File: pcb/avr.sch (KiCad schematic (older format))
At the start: 36 parts, among them IC201 MCU-ATMEGA328P-MU_QFN32_, J201 CONN_02X03, J202 jumper, P201 CONNECTOR, P202 CONNECTOR, P203 CONNECTOR, P204 CONNECTOR, P205 CONNECTOR, P206 CONNECTOR, P207 CONNECTOR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

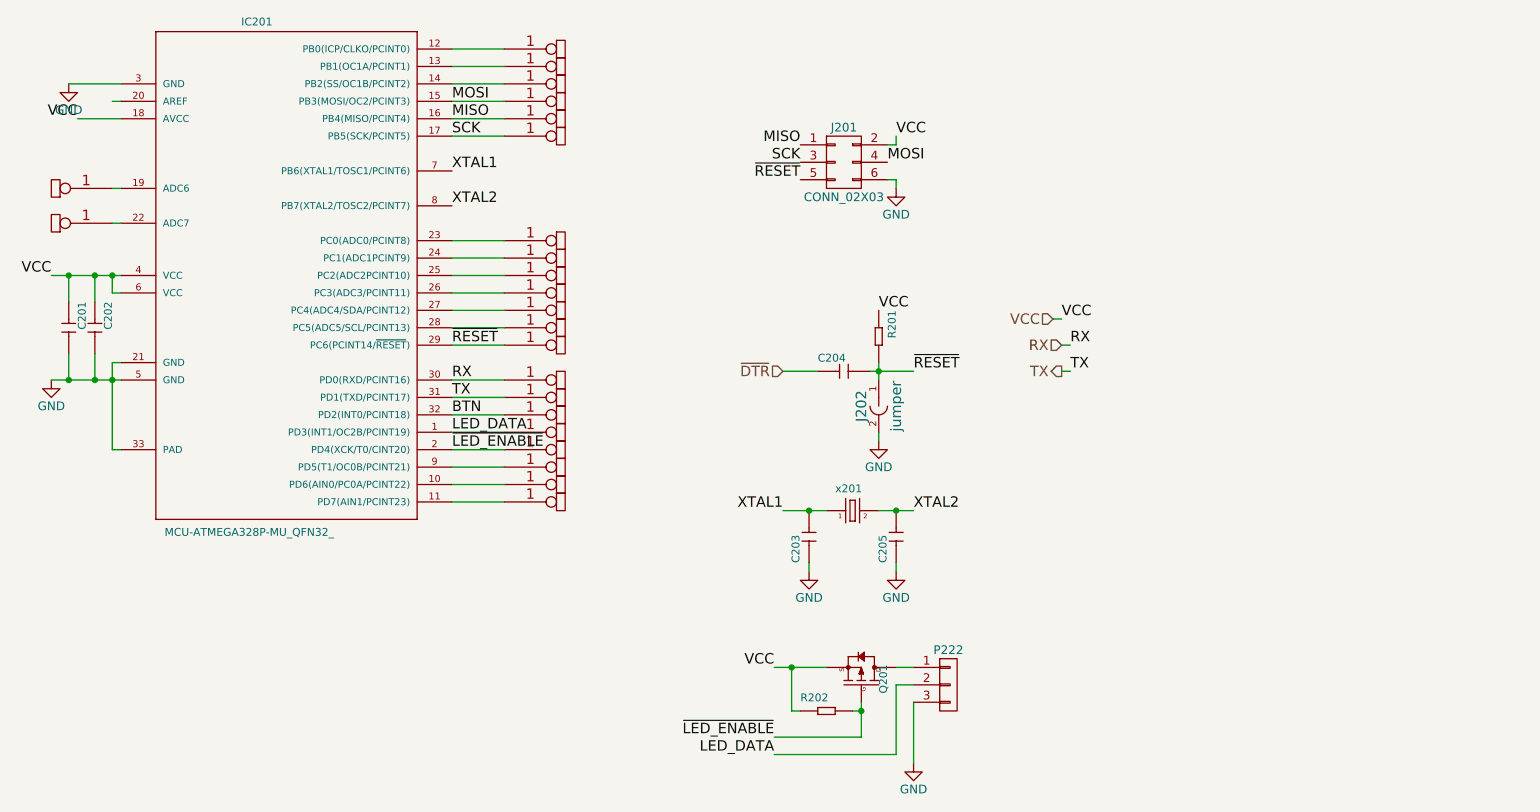
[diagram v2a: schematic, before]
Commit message: added button, capacitor to led strip power and jumpers to external rx/tx. everything layed out and connected
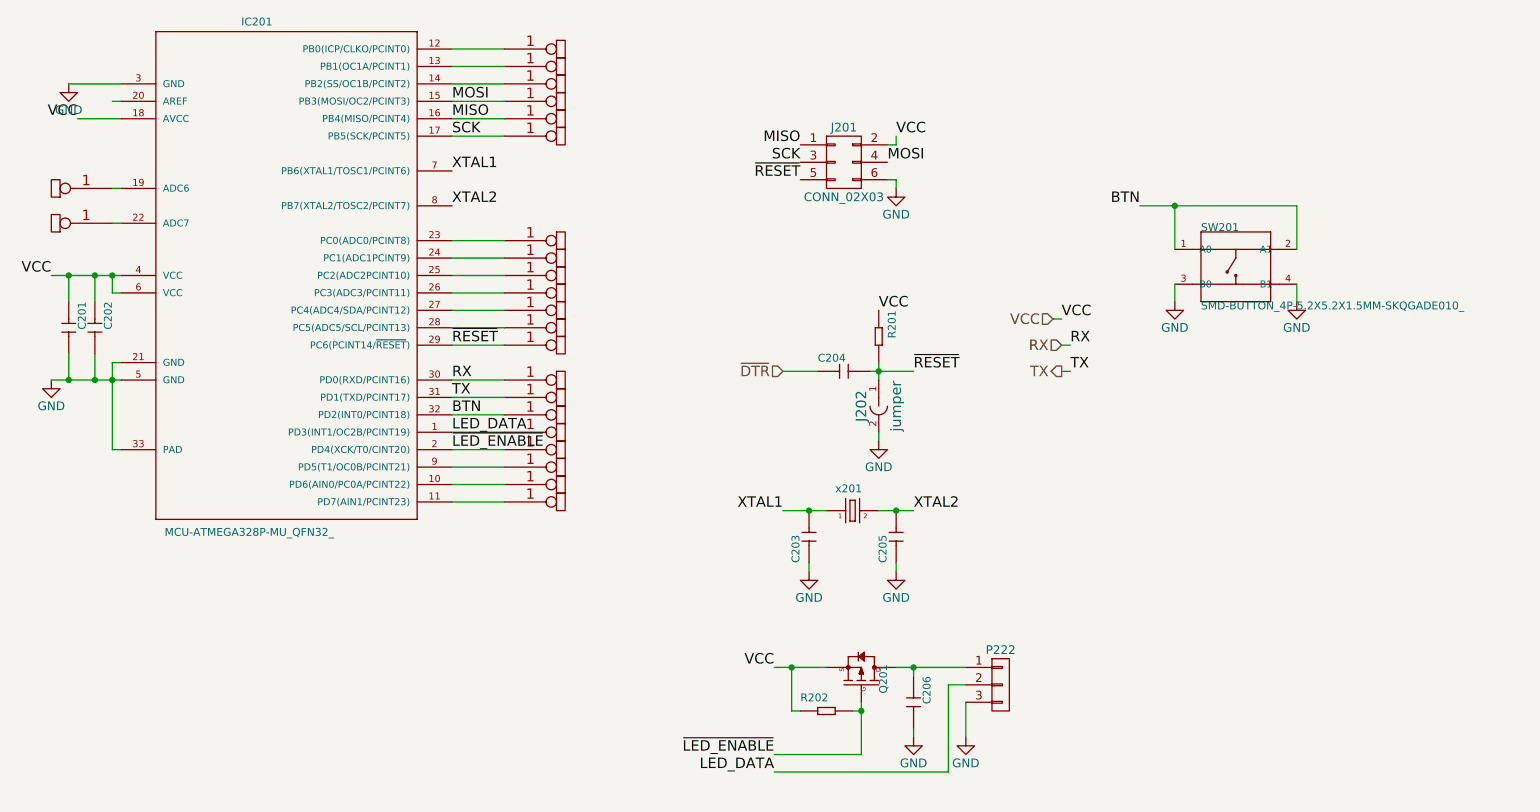
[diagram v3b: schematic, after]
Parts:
- added C206: CERAMIC-22UF-6.3V-20%-X5R_0805_, netl:C0805, symbol CERAMIC-22UF-6.3V-20%-X5R_0805_
- added SW201: SMD-BUTTON_4P-5.2X5.2X1.5MM-SKQGADE010_, SeeedOPL-Switch-2016:SW4-SMD-5.2X5.2X1.5MM, symbol SMD-BUTTON_4P-5.2X5.2X1.5MM-SKQGADE010_
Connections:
- net BTN: now also SW201.1 (A0), SW201.2 (A1)
- net GND: now also C206.2, SW201.3 (B0), SW201.4 (B1)
- net at P222.1 (P1), Q201.3 (D): now also C206.1
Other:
- moved on the sheet: P222
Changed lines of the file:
@@
 L CONN_01X03 P222
 U 1 1 58BAB28B
-P 8250 5800
-F 0 "P222" H 8250 6000 50  0000 C CNN
-F 1 "CONN_01X03" V 8350 5800 50  0001 C CNN
-F 2 "netl:SM_3_WIRE" H 8250 5800 50  0001 C CNN
-F 3 "" H 8250 5800 50  0000 C CNN
-	1    8250 5800
-	1    0    0    -1
-$EndComp
-$Comp
-L GND #PWR207
+P 8550 5800
+F 0 "P222" H 8550 6000 50  0000 C CNN
+F 1 "CONN_01X03" V 8650 5800 50  0001 C CNN
+F 2 "netl:SM_3_WIRE" H 8550 5800 50  0001 C CNN
+F 3 "" H 8550 5800 50  0000 C CNN
+	1    8550 5800
+	1    0    0    -1
+$EndComp
+$Comp
+L GND #PWR05
 U 1 1 58BAB3DE
-P 8050 6250
-F 0 "#PWR207" H 8050 6000 50  0001 C CNN
-F 1 "GND" H 8050 6100 50  0000 C CNN
-F 2 "" H 8050 6250 50  0000 C CNN
-F 3 "" H 8050 6250 50  0000 C CNN
-	1    8050 6250
-	1    0    0    -1
-$EndComp
-Text Label 7250 6200 2    60   ~ 0
+P 8350 6100
+F 0 "#PWR05" H 8350 5850 50  0001 C CNN
+F 1 "GND" H 8350 5950 50  0000 C CNN
+F 2 "" H 8350 6100 50  0000 C CNN
+F 3 "" H 8350 6100 50  0000 C CNN
+	1    8350 6100
+	1    0    0    -1
+$EndComp
+Text Label 7250 6300 2    60   ~ 0
 LED_DATA
 $Comp
@@
 $EndComp
 $Comp
-L GND #PWR206
+L GND #PWR06
 U 1 1 5A3AC4B3
 P 7950 5150
-F 0 "#PWR206" H 7950 4900 50  0001 C CNN
+F 0 "#PWR06" H 7950 4900 50  0001 C CNN
 F 1 "GND" H 7950 5000 50  0000 C CNN
 F 2 "" H 7950 5150 50  0000 C CNN
@@
 $EndComp
 $Comp
-L GND #PWR203
+L GND #PWR07
 U 1 1 5A3AC530
 P 7450 5150
-F 0 "#PWR203" H 7450 4900 50  0001 C CNN
+F 0 "#PWR07" H 7450 4900 50  0001 C CNN
 F 1 "GND" H 7450 5000 50  0000 C CNN
 F 2 "" H 7450 5150 50  0000 C CNN
@@
 $EndComp
 $Comp
-L GND #PWR201
+L GND #PWR08
 U 1 1 5A3AD1F6
 P 3100 4050
-F 0 "#PWR201" H 3100 3800 50  0001 C CNN
+F 0 "#PWR08" H 3100 3800 50  0001 C CNN
 F 1 "GND" H 3100 3900 50  0000 C CNN
 F 2 "" H 3100 4050 50  0001 C CNN
@@
 $EndComp
 $Comp
-L GND #PWR202
+L GND #PWR09
 U 1 1 5A3AE5DA
 P 3200 2350
-F 0 "#PWR202" H 3200 2100 50  0001 C CNN
+F 0 "#PWR09" H 3200 2100 50  0001 C CNN
 F 1 "GND" H 3200 2200 50  0000 C CNN
 F 2 "" H 3200 2350 50  0001 C CNN
@@
 SCK
 $Comp
-L GND #PWR205
+L GND #PWR010
 U 1 1 5A551E4E
 P 7950 2950
-F 0 "#PWR205" H 7950 2700 50  0001 C CNN
+F 0 "#PWR010" H 7950 2700 50  0001 C CNN
 F 1 "GND" H 7950 2800 50  0000 C CNN
 F 2 "" H 7950 2950 50  0000 C CNN
@@
 	1    0    0    -1
 $EndComp
-Wire Wire Line
-	8050 5900 8050 6250
-Wire Wire Line
-	7950 5800 8050 5800
-Wire Wire Line
-	7950 5700 8050 5700
-Wire Wire Line
-	7300 4800 7550 4800
-Wire Wire Line
-	7850 4800 8050 4800
-Wire Wire Line
-	7450 5100 7450 5150
-Wire Wire Line
-	7950 5100 7950 5150
-Connection ~ 7450 4800
-Connection ~ 7950 4800
-Wire Wire Line
-	3100 3450 3500 3450
-Wire Wire Line
-	3200 3600 3200 3450
-Connection ~ 3200 3450
-Wire Wire Line
-	3350 3600 3350 3450
-Connection ~ 3350 3450
-Wire Wire Line
-	3500 3550 3450 3550
-Wire Wire Line
-	3450 3550 3450 3450
-Connection ~ 3450 3450
-Wire Wire Line
-	3100 4050 3500 4050
-Wire Wire Line
-	3200 3900 3200 4050
-Connection ~ 3200 4050
-Wire Wire Line
-	3350 3900 3350 4050
-Connection ~ 3350 4050
-Wire Wire Line
-	3500 3950 3450 3950
-Wire Wire Line
-	3450 3950 3450 4450
-Connection ~ 3450 4050
-Wire Wire Line
-	3500 2350 3200 2350
-Wire Wire Line
-	5400 4050 5700 4050
-Wire Wire Line
-	5400 4150 5700 4150
-Wire Wire Line
-	7850 3950 7850 4050
-Wire Wire Line
-	7800 4000 8050 4000
-Connection ~ 7850 4000
-Wire Wire Line
-	7500 4000 7300 4000
-Wire Wire Line
-	5700 4250 5400 4250
-Wire Wire Line
-	5400 4350 5700 4350
-Wire Wire Line
-	5700 4450 5400 4450
-Wire Wire Line
-	5400 4550 5700 4550
-Wire Wire Line
-	5700 4650 5400 4650
-Wire Wire Line
-	5400 4750 5700 4750
-Wire Wire Line
-	5400 3850 5700 3850
-Wire Wire Line
-	5400 3750 5700 3750
-Wire Wire Line
-	5700 3650 5400 3650
-Wire Wire Line
-	5400 3550 5700 3550
-Wire Wire Line
-	5700 3450 5400 3450
-Wire Wire Line
-	5400 3350 5700 3350
-Wire Wire Line
-	5700 3250 5400 3250
-Wire Wire Line
-	5400 2650 5700 2650
-Wire Wire Line
-	5700 2550 5400 2550
-Wire Wire Line
-	5400 2450 5700 2450
-Wire Wire Line
-	5700 2350 5400 2350
-Wire Wire Line
-	5400 2250 5700 2250
-Wire Wire Line
-	5700 2150 5400 2150
-Wire Wire Line
-	3500 2950 3450 2950
-Wire Wire Line
-	3450 3150 3500 3150
-Wire Wire Line
-	8900 3850 8950 3850
-Wire Wire Line
-	8900 4000 8950 4000
-Wire Wire Line
-	3450 4450 3500 4450
-Wire Wire Line
-	7950 2950 7950 2900
-Wire Wire Line
-	7950 2900 7900 2900
-Wire Wire Line
-	7950 2650 7950 2700
-Wire Wire Line
-	7950 2700 7900 2700
-Wire Wire Line
-	8850 3700 8900 3700
-Wire Wire Line
-	7250 5700 7550 5700
-Wire Wire Line
-	7750 5900 7750 6100
-Wire Wire Line
-	7750 5950 7700 5950
-Wire Wire Line
-	7400 5950 7350 5950
-Wire Wire Line
-	7350 5950 7350 5700
-Connection ~ 7350 5700
-Wire Wire Line
-	7750 6100 7250 6100
-Connection ~ 7750 5950
-Text Label 7250 6100 2    60   ~ 0
+Text Label 7250 6200 2    60   ~ 0
 ~LED_ENABLE
 Text Label 5400 4450 0    60   ~ 0
@@
 $EndComp
 $Comp
-L GND #PWR204
+L GND #PWR011
 U 1 1 5A566D1F
 P 7850 4400
-F 0 "#PWR204" H 7850 4150 50  0001 C CNN
+F 0 "#PWR011" H 7850 4150 50  0001 C CNN
 F 1 "GND" H 7850 4250 50  0000 C CNN
 F 2 "" H 7850 4400 50  0000 C CNN
@@
 	1    0    0    -1
 $EndComp
+$Comp
+L SMD-BUTTON_4P-5.2X5.2X1.5MM-SKQGADE010_ SW201
+U 1 1 5A78AF11
+P 9900 3400
+F 0 "SW201" H 9700 3600 45  0000 L BNN
+F 1 "SMD-BUTTON_4P-5.2X5.2X1.5MM-SKQGADE010_" H 9700 3150 45  0000 L BNN
+F 2 "SeeedOPL-Switch-2016:SW4-SMD-5.2X5.2X1.5MM" H 9900 3400 60  0001 C CNN
+F 3 "" H 9900 3400 60  0001 C CNN
+F 4 "SKQGADE010" H 9930 3550 20  0001 C CNN "MPN"
+F 5 "311020017" H 9930 3550 20  0001 C CNN "SKU"
+	1    9900 3400
+	1    0    0    -1
+$EndComp
+Wire Wire Line
+	8350 5900 8350 6100
+Wire Wire Line
+	8250 5800 8350 5800
+Wire Wire Line
+	7950 5700 8350 5700
+Wire Wire Line
+	7300 4800 7550 4800
+Wire Wire Line
+	7850 4800 8050 4800
+Wire Wire Line
+	7450 5100 7450 5150
+Wire Wire Line
+	7950 5100 7950 5150
+Connection ~ 7450 4800
+Connection ~ 7950 4800
+Wire Wire Line
+	3100 3450 3500 3450
+Wire Wire Line
+	3200 3600 3200 3450
+Connection ~ 3200 3450
+Wire Wire Line
+	3350 3600 3350 3450
+Connection ~ 3350 3450
+Wire Wire Line
+	3500 3550 3450 3550
+Wire Wire Line
+	3450 3550 3450 3450
+Connection ~ 3450 3450
+Wire Wire Line
+	3100 4050 3500 4050
+Wire Wire Line
+	3200 3900 3200 4050
+Connection ~ 3200 4050
+Wire Wire Line
+	3350 3900 3350 4050
+Connection ~ 3350 4050
+Wire Wire Line
+	3500 3950 3450 3950
+Wire Wire Line
+	3450 3950 3450 4450
+Connection ~ 3450 4050
+Wire Wire Line
+	3500 2350 3200 2350
+Wire Wire Line
+	5400 4050 5700 4050
+Wire Wire Line
+	5400 4150 5700 4150
+Wire Wire Line
+	7850 3950 7850 4050
+Wire Wire Line
+	7800 4000 8050 4000
+Connection ~ 7850 4000
+Wire Wire Line
+	7500 4000 7300 4000
+Wire Wire Line
+	5700 4250 5400 4250
+Wire Wire Line
+	5400 4350 5700 4350
+Wire Wire Line
+	5700 4450 5400 4450
+Wire Wire Line
+	5400 4550 5700 4550
+Wire Wire Line
+	5700 4650 5400 4650
+Wire Wire Line
+	5400 4750 5700 4750
+Wire Wire Line
+	5400 3850 5700 3850
+Wire Wire Line
+	5400 3750 5700 3750
+Wire Wire Line
+	5700 3650 5400 3650
+Wire Wire Line
+	5400 3550 5700 3550
+Wire Wire Line
+	5700 3450 5400 3450
+Wire Wire Line
+	5400 3350 5700 3350
+Wire Wire Line
+	5700 3250 5400 3250
+Wire Wire Line
+	5400 2650 5700 2650
+Wire Wire Line
+	5700 2550 5400 2550
+Wire Wire Line
+	5400 2450 5700 2450
+Wire Wire Line
+	5700 2350 5400 2350
+Wire Wire Line
+	5400 2250 5700 2250
+Wire Wire Line
+	5700 2150 5400 2150
+Wire Wire Line
+	3500 2950 3450 2950
+Wire Wire Line
+	3450 3150 3500 3150
+Wire Wire Line
+	8900 3850 8950 3850
+Wire Wire Line
+	8900 4000 8950 4000
+Wire Wire Line
+	3450 4450 3500 4450
+Wire Wire Line
+	7950 2950 7950 2900
+Wire Wire Line
+	7950 2900 7900 2900
+Wire Wire Line
+	7950 2650 7950 2700
+Wire Wire Line
+	7950 2700 7900 2700
+Wire Wire Line
+	8850 3700 8900 3700
+Wire Wire Line
+	7250 5700 7550 5700
+Wire Wire Line
+	7750 5900 7750 6200
+Wire Wire Line
+	7750 5950 7700 5950
+Wire Wire Line
+	7400 5950 7350 5950
+Wire Wire Line
+	7350 5950 7350 5700
+Connection ~ 7350 5700
+Wire Wire Line
+	7750 6200 7250 6200
+Connection ~ 7750 5950
 Wire Wire Line
 	7850 4350 7850 4400
 Wire Wire Line
-	7250 6200 7950 6200
-Wire Wire Line
-	7950 6200 7950 5800
+	7250 6300 8250 6300
+Wire Wire Line
+	8250 6300 8250 5800
 Wire Wire Line
 	3250 2550 3500 2550
 Wire Wire Line
 	3500 2450 3450 2450
+Wire Wire Line
+	10250 3050 10250 3300
+Wire Wire Line
+	9350 3050 10250 3050
+Wire Wire Line
+	9550 3050 9550 3300
+Connection ~ 9550 3050
+Text Label 9350 3050 2    60   ~ 0
+BTN
+$Comp
+L GND #PWR012
+U 1 1 5A78B21A
+P 9550 3600
+F 0 "#PWR012" H 9550 3350 50  0001 C CNN
+F 1 "GND" H 9550 3450 50  0000 C CNN
+F 2 "" H 9550 3600 50  0000 C CNN
+F 3 "" H 9550 3600 50  0000 C CNN
+	1    9550 3600
+	1    0    0    -1
+$EndComp
+$Comp
+L GND #PWR013
+U 1 1 5A78B24F
+P 10250 3600
+F 0 "#PWR013" H 10250 3350 50  0001 C CNN
+F 1 "GND" H 10250 3450 50  0000 C CNN
+F 2 "" H 10250 3600 50  0000 C CNN
+F 3 "" H 10250 3600 50  0000 C CNN
+	1    10250 3600
+	1    0    0    -1
+$EndComp
+Wire Wire Line
+	10250 3500 10250 3600
+Wire Wire Line
+	9550 3500 9550 3600
+$Comp
+L CERAMIC-22UF-6.3V-20%-X5R_0805_ C206
+U 1 1 5A78E537
+P 8050 5900
+F 0 "C206" H 7900 5950 45  0000 L BNN
+F 1 "CERAMIC-22UF-6.3V-20%-X5R_0805_" H 7900 5800 45  0001 L BNN
+F 2 "netl:C0805" H 8050 5900 60  0001 C CNN
+F 3 "" H 8050 5900 60  0001 C CNN
+F 4 "CC0805MKX5R5BB226" H 8080 6050 20  0001 C CNN "MPN"
+F 5 "302010171" H 8080 6050 20  0001 C CNN "SKU"
+	1    8050 5900
+	0    1    1    0
+$EndComp
+$Comp
+L GND #PWR014
+U 1 1 5A78E7FE
+P 8050 6100
+F 0 "#PWR014" H 8050 5850 50  0001 C CNN
+F 1 "GND" H 8050 5950 50  0000 C CNN
+F 2 "" H 8050 6100 50  0000 C CNN
+F 3 "" H 8050 6100 50  0000 C CNN
+	1    8050 6100
+	1    0    0    -1
+$EndComp
+Wire Wire Line
+	8050 6100 8050 6050
+Wire Wire Line
+	8050 5750 8050 5700
+Connection ~ 8050 5700
 $EndSCHEMATC
